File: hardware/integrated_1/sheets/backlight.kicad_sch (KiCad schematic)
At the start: 6 parts

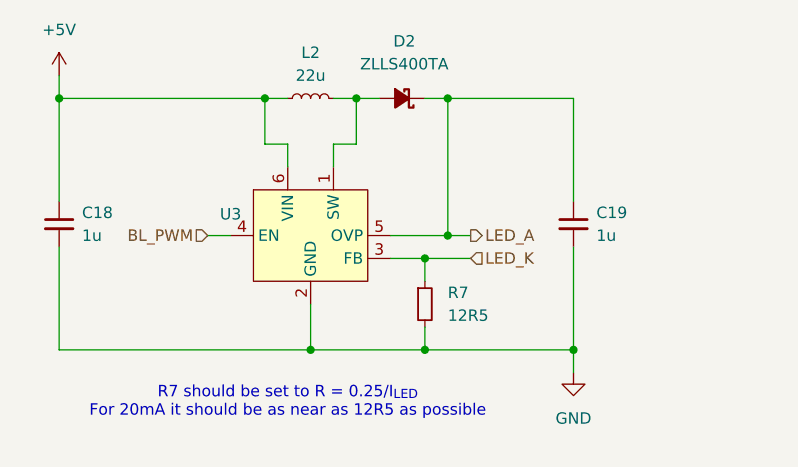
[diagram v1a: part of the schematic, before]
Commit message: automatic kicad reference update
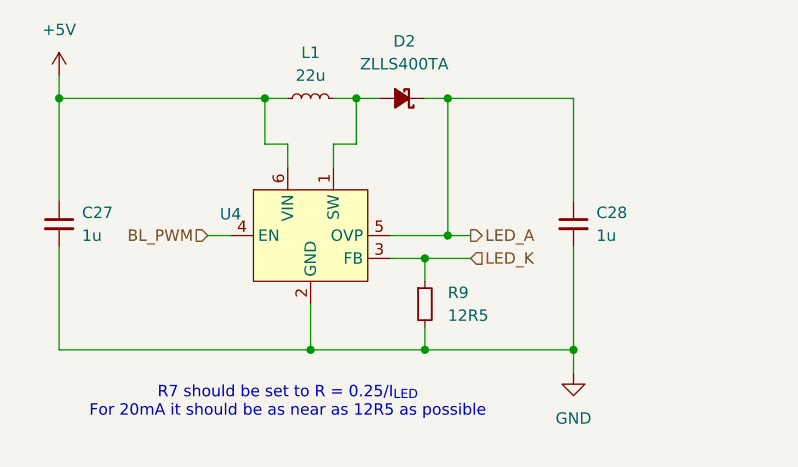
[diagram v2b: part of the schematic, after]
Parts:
- R9: renamed from R7; footprint Resistor_SMD:R_0603_1608Metric -> Resistor_SMD:R_0402_1005Metric
- renumbered C18 to C27, C19 to C28, L2 to L1, U3 to U4
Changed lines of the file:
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@@
 		(dnp no)
 		(fields_autoplaced yes)
-		(property "Reference" "#PWR026"
+		(property "Reference" "#PWR041"
 			(at 336.55 217.17 0)
 			(effects
@@
 			(project "integrated_1"
 				(path "/5cc60e42-d666-4a43-b4f0-3784ee4bf951/7e4f175d-d60a-4b23-9cf2-ca90d4a48e7e"
-					(reference "#PWR026")
+					(reference "#PWR041")
 					(unit 1)
 				)
@@
 		(dnp no)
 		(fields_autoplaced yes)
-		(property "Reference" "C18"
+		(property "Reference" "C27"
 			(at 116.84 93.9862 0)
 			(effects
@@
 			(project "integrated_1"
 				(path "/5cc60e42-d666-4a43-b4f0-3784ee4bf951/7e4f175d-d60a-4b23-9cf2-ca90d4a48e7e"
-					(reference "C18")
+					(reference "C27")
 					(unit 1)
 				)
@@
 		(dnp no)
 		(fields_autoplaced yes)
-		(property "Reference" "R7"
+		(property "Reference" "R9"
 			(at 157.48 102.8699 0)
 			(effects
@@
 			)
 		)
-		(property "Footprint" "Resistor_SMD:R_0603_1608Metric"
+		(property "Footprint" "Resistor_SMD:R_0402_1005Metric"
 			(at 154.94 104.14 0)
 			(effects
@@
 			(project "integrated_1"
 				(path "/5cc60e42-d666-4a43-b4f0-3784ee4bf951/7e4f175d-d60a-4b23-9cf2-ca90d4a48e7e"
-					(reference "R7")
+					(reference "R9")
 					(unit 1)
 				)
@@
 		(dnp no)
 		(fields_autoplaced yes)
-		(property "Reference" "#PWR025"
+		(property "Reference" "#PWR039"
 			(at 114.3 82.55 0)
 			(effects
@@
 			(project "integrated_1"
 				(path "/5cc60e42-d666-4a43-b4f0-3784ee4bf951/7e4f175d-d60a-4b23-9cf2-ca90d4a48e7e"
-					(reference "#PWR025")
+					(reference "#PWR039")
 					(unit 1)
 				)
@@
 		(dnp no)
 		(fields_autoplaced yes)
-		(property "Reference" "#PWR027"
+		(property "Reference" "#PWR040"
 			(at 171.45 118.11 0)
 			(effects
@@
 			(project "integrated_1"
 				(path "/5cc60e42-d666-4a43-b4f0-3784ee4bf951/7e4f175d-d60a-4b23-9cf2-ca90d4a48e7e"
-					(reference "#PWR027")
+					(reference "#PWR040")
 					(unit 1)
 				)
@@
 		(dnp no)
 		(fields_autoplaced yes)
-		(property "Reference" "L2"
+		(property "Reference" "L1"
 			(at 142.24 76.2 90)
 			(effects
@@
 			(project "integrated_1"
 				(path "/5cc60e42-d666-4a43-b4f0-3784ee4bf951/7e4f175d-d60a-4b23-9cf2-ca90d4a48e7e"
-					(reference "L2")
+					(reference "L1")
 					(unit 1)
 				)
@@
 		(dnp no)
 		(fields_autoplaced yes)
-		(property "Reference" "C19"
+		(property "Reference" "C28"
 			(at 173.99 93.9862 0)
 			(effects
@@
 			(project "integrated_1"
 				(path "/5cc60e42-d666-4a43-b4f0-3784ee4bf951/7e4f175d-d60a-4b23-9cf2-ca90d4a48e7e"
-					(reference "C19")
+					(reference "C28")
 					(unit 1)
 				)
@@
 		(dnp no)
 		(fields_autoplaced yes)
-		(property "Reference" "U3"
+		(property "Reference" "U4"
 			(at 133.35 94.142 0)
 			(effects
@@
 			(project "integrated_1"
 				(path "/5cc60e42-d666-4a43-b4f0-3784ee4bf951/7e4f175d-d60a-4b23-9cf2-ca90d4a48e7e"
-					(reference "U3")
-					(unit 1)
-				)
+					(reference "U4")
+					(unit 1)
+				)

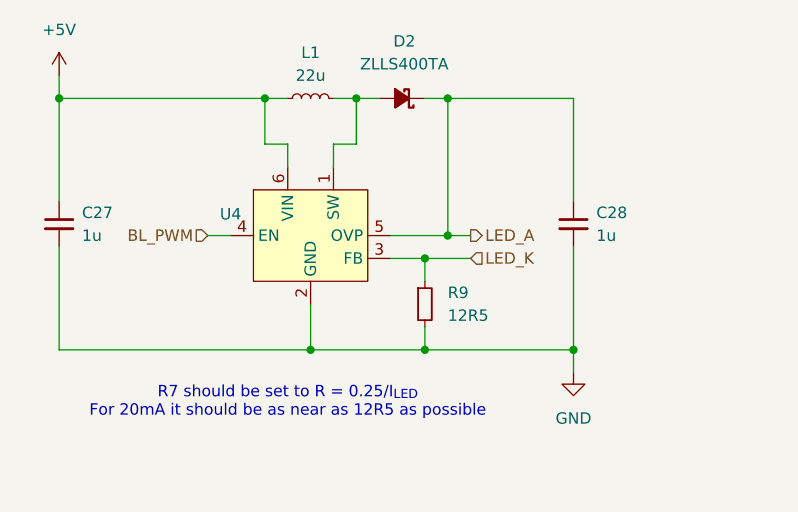
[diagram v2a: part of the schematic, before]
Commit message: reannotated schematic
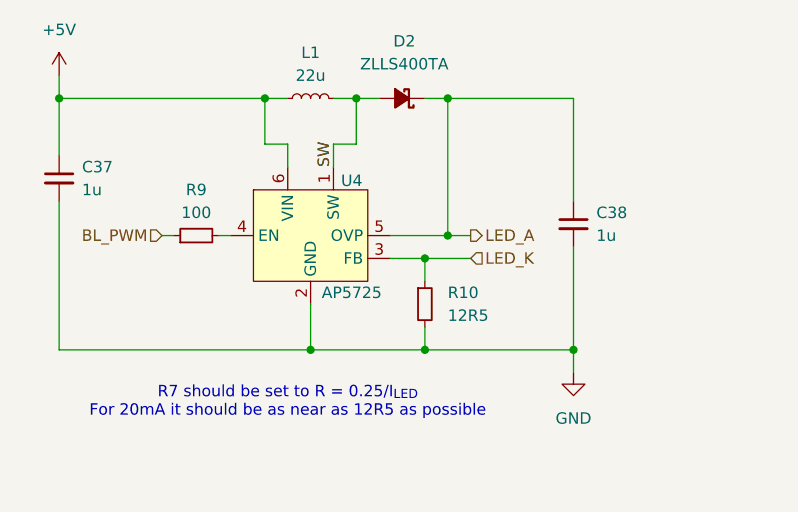
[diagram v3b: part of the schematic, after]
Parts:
- added R9: 100, KiCAD Library:R_0402_1005Metric, symbol Device:R_Small
- C37: renamed from C27; footprint Capacitor_SMD:C_0603_1608Metric -> KiCAD Library:C_0402_1005Metric
- C38: renamed from C28; footprint Capacitor_SMD:C_0603_1608Metric -> KiCAD Library:C_0603_1608Metric
- D2: footprint (none) -> Diode_SMD:D_SOD-323
- L1: footprint (none) -> KiCAD Library:XRNR4012
- R10: renamed from R9; footprint Resistor_SMD:R_0402_1005Metric -> KiCAD Library:R_0402_1005Metric
- U4: value ~ -> AP5725
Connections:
- net BL_PWM: now also R9.1; no longer U4.4 (EN)
- net SW: now reaches D2.2 (A), L1.2, U4.1 (SW)
- new net: R9.2, U4.4 (EN)
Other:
- moved on the sheet: C37
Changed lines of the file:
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@@
 	(wire
 		(pts
-			(xy 130.81 96.52) (xy 133.35 96.52)
+			(xy 125.73 96.52) (xy 127 96.52)
 		)
 		(stroke
@@
 	(wire
 		(pts
-			(xy 114.3 97.79) (xy 114.3 109.22)
+			(xy 114.3 92.71) (xy 114.3 109.22)
 		)
 		(stroke
@@
 	(wire
 		(pts
+			(xy 132.08 96.52) (xy 133.35 96.52)
+		)
+		(stroke
+			(width 0)
+			(type default)
+		)
+	)
+	(wire
+		(pts
 			(xy 171.45 109.22) (xy 154.94 109.22)
 		)
@@
 	(wire
 		(pts
-			(xy 114.3 81.28) (xy 114.3 92.71)
+			(xy 114.3 81.28) (xy 114.3 87.63)
 		)
 		(stroke
@@
 		)
 	)
+	(label "SW"
+		(at 144.78 88.9 90)
+		(fields_autoplaced yes)
+		(effects
+			(font
+				(size 1.27 1.27)
+			)
+			(justify left bottom)
+		)
+	)
 	(hierarchical_label "LED_A"
 		(shape output)
@@
 	(hierarchical_label "BL_PWM"
 		(shape input)
-		(at 130.81 96.52 180)
+		(at 125.73 96.52 180)
 		(fields_autoplaced yes)
 		(effects
@@
 		(dnp no)
 		(fields_autoplaced yes)
-		(property "Reference" "#PWR041"
+		(property "Reference" "#PWR037"
 			(at 336.55 217.17 0)
 			(effects
@@
 			(project "integrated_1"
 				(path "/5cc60e42-d666-4a43-b4f0-3784ee4bf951/7e4f175d-d60a-4b23-9cf2-ca90d4a48e7e"
-					(reference "#PWR041")
+					(reference "#PWR037")
 					(unit 1)
 				)
@@
 			)
 		)
-		(property "Footprint" ""
+		(property "Footprint" "Diode_SMD:D_SOD-323"
 			(at 152.4 81.28 90)
 			(effects
@@
 	(symbol
 		(lib_id "Device:C_Small")
-		(at 114.3 95.25 0)
-		(unit 1)
-		(exclude_from_sim no)
-		(in_bom yes)
-		(on_board yes)
-		(dnp no)
-		(fields_autoplaced yes)
-		(property "Reference" "C27"
-			(at 116.84 93.9862 0)
+		(at 114.3 90.17 0)
+		(unit 1)
+		(exclude_from_sim no)
+		(in_bom yes)
+		(on_board yes)
+		(dnp no)
+		(fields_autoplaced yes)
+		(property "Reference" "C37"
+			(at 116.84 88.9062 0)
 			(effects
 				(font
@@
 		)
 		(property "Value" "1u"
-			(at 116.84 96.5262 0)
+			(at 116.84 91.4462 0)
 			(effects
 				(font
@@
 			)
 		)
-		(property "Footprint" "Capacitor_SMD:C_0603_1608Metric"
-			(at 114.3 95.25 0)
+		(property "Footprint" "KiCAD Library:C_0402_1005Metric"
+			(at 114.3 90.17 0)
 			(effects
 				(font
@@
 		)
 		(property "Datasheet" "~"
-			(at 114.3 95.25 0)
+			(at 114.3 90.17 0)
 			(effects
 				(font
@@
 		)
 		(property "Description" "Unpolarized capacitor, small symbol"
-			(at 114.3 95.25 0)
+			(at 114.3 90.17 0)
 			(effects
 				(font
@@
 			(project "integrated_1"
 				(path "/5cc60e42-d666-4a43-b4f0-3784ee4bf951/7e4f175d-d60a-4b23-9cf2-ca90d4a48e7e"
-					(reference "C27")
+					(reference "C37")
 					(unit 1)
 				)
@@
 		(dnp no)
 		(fields_autoplaced yes)
-		(property "Reference" "R9"
+		(property "Reference" "R10"
 			(at 157.48 102.8699 0)
 			(effects
@@
 			)
 		)
-		(property "Footprint" "Resistor_SMD:R_0402_1005Metric"
+		(property "Footprint" "KiCAD Library:R_0402_1005Metric"
 			(at 154.94 104.14 0)
 			(effects
@@
 		(property "Description" "Resistor, small symbol"
 			(at 154.94 104.14 0)
+			(effects
+				(font
+					(size 1.27 1.27)
+				)
+				(hide yes)
+			)
+		)
+		(pin "2"
+		)
+		(pin "1"
+		)
+		(instances
+			(project "integrated_1"
+				(path "/5cc60e42-d666-4a43-b4f0-3784ee4bf951/7e4f175d-d60a-4b23-9cf2-ca90d4a48e7e"
+					(reference "R10")
+					(unit 1)
+				)
+			)
+		)
+	)
+	(symbol
+		(lib_id "Device:R_Small")
+		(at 129.54 96.52 90)
+		(unit 1)
+		(exclude_from_sim no)
+		(in_bom yes)
+		(on_board yes)
+		(dnp no)
+		(fields_autoplaced yes)
+		(property "Reference" "R9"
+			(at 129.54 91.44 90)
+			(effects
+				(font
+					(size 1.27 1.27)
+				)
+			)
+		)
+		(property "Value" "100"
+			(at 129.54 93.98 90)
+			(effects
+				(font
+					(size 1.27 1.27)
+				)
+			)
+		)
+		(property "Footprint" "KiCAD Library:R_0402_1005Metric"
+			(at 129.54 96.52 0)
+			(effects
+				(font
+					(size 1.27 1.27)
+				)
+				(hide yes)
+			)
+		)
+		(property "Datasheet" "~"
+			(at 129.54 96.52 0)
+			(effects
+				(font
+					(size 1.27 1.27)
+				)
+				(hide yes)
+			)
+		)
+		(property "Description" "Resistor, small symbol"
+			(at 129.54 96.52 0)
 			(effects
 				(font
@@
 		(dnp no)
 		(fields_autoplaced yes)
-		(property "Reference" "#PWR039"
+		(property "Reference" "#PWR035"
 			(at 114.3 82.55 0)
 			(effects
@@
 			(project "integrated_1"
 				(path "/5cc60e42-d666-4a43-b4f0-3784ee4bf951/7e4f175d-d60a-4b23-9cf2-ca90d4a48e7e"
-					(reference "#PWR039")
+					(reference "#PWR035")
 					(unit 1)
 				)
@@
 		(dnp no)
 		(fields_autoplaced yes)
-		(property "Reference" "#PWR040"
+		(property "Reference" "#PWR036"
 			(at 171.45 118.11 0)
 			(effects
@@
 			(project "integrated_1"
 				(path "/5cc60e42-d666-4a43-b4f0-3784ee4bf951/7e4f175d-d60a-4b23-9cf2-ca90d4a48e7e"
-					(reference "#PWR040")
+					(reference "#PWR036")
 					(unit 1)
 				)
@@
 			)
 		)
-		(property "Footprint" ""
+		(property "Footprint" "KiCAD Library:XRNR4012"
 			(at 142.24 81.28 0)
 			(effects
@@
 		(dnp no)
 		(fields_autoplaced yes)
-		(property "Reference" "C28"
+		(property "Reference" "C38"
 			(at 173.99 93.9862 0)
 			(effects
@@
 			)
 		)
-		(property "Footprint" "Capacitor_SMD:C_0603_1608Metric"
+		(property "Footprint" "KiCAD Library:C_0603_1608Metric"
 			(at 171.45 95.25 0)
 			(effects
@@
 			(project "integrated_1"
 				(path "/5cc60e42-d666-4a43-b4f0-3784ee4bf951/7e4f175d-d60a-4b23-9cf2-ca90d4a48e7e"
-					(reference "C28")
+					(reference "C38")
 					(unit 1)
 				)
@@
 		(on_board yes)
 		(dnp no)
-		(fields_autoplaced yes)
 		(property "Reference" "U4"
-			(at 133.35 94.142 0)
-			(effects
-				(font
-					(size 1.27 1.27)
-				)
-			)
-		)
-		(property "Value" "~"
-			(at 133.35 96.0471 0)
-			(effects
-				(font
+			(at 146.812 90.424 0)
+			(effects
+				(font
+					(size 1.27 1.27)
+				)
+			)
+		)
+		(property "Value" "AP5725"
+			(at 146.812 102.87 0)
+			(effects
+				(font

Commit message: reannotated
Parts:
- renumbered C37 to C41, C38 to C42, D2 to D10, R9 to R11, R10 to R12, U4 to U6
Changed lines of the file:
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@@
 		(dnp no)
 		(fields_autoplaced yes)
-		(property "Reference" "#PWR037"
+		(property "Reference" "#PWR048"
 			(at 336.55 217.17 0)
 			(effects
@@
 			(project "integrated_1"
 				(path "/5cc60e42-d666-4a43-b4f0-3784ee4bf951/7e4f175d-d60a-4b23-9cf2-ca90d4a48e7e"
-					(reference "#PWR037")
+					(reference "#PWR048")
 					(unit 1)
 				)
@@
 		(dnp no)
 		(fields_autoplaced yes)
-		(property "Reference" "D2"
+		(property "Reference" "D10"
 			(at 152.654 74.93 0)
 			(effects
@@
 			(project "integrated_1"
 				(path "/5cc60e42-d666-4a43-b4f0-3784ee4bf951/7e4f175d-d60a-4b23-9cf2-ca90d4a48e7e"
-					(reference "D2")
+					(reference "D10")
 					(unit 1)
 				)
@@
 		(dnp no)
 		(fields_autoplaced yes)
-		(property "Reference" "C37"
+		(property "Reference" "C41"
 			(at 116.84 88.9062 0)
 			(effects
@@
 			(project "integrated_1"
 				(path "/5cc60e42-d666-4a43-b4f0-3784ee4bf951/7e4f175d-d60a-4b23-9cf2-ca90d4a48e7e"
-					(reference "C37")
+					(reference "C41")
 					(unit 1)
 				)
@@
 		(dnp no)
 		(fields_autoplaced yes)
-		(property "Reference" "R10"
+		(property "Reference" "R12"
 			(at 157.48 102.8699 0)
 			(effects
@@
 			(project "integrated_1"
 				(path "/5cc60e42-d666-4a43-b4f0-3784ee4bf951/7e4f175d-d60a-4b23-9cf2-ca90d4a48e7e"
-					(reference "R10")
+					(reference "R12")
 					(unit 1)
 				)
@@
 		(dnp no)
 		(fields_autoplaced yes)
-		(property "Reference" "R9"
+		(property "Reference" "R11"
 			(at 129.54 91.44 90)
 			(effects
@@
 			(project "integrated_1"
 				(path "/5cc60e42-d666-4a43-b4f0-3784ee4bf951/7e4f175d-d60a-4b23-9cf2-ca90d4a48e7e"
-					(reference "R9")
+					(reference "R11")
 					(unit 1)
 				)
@@
 		(dnp no)
 		(fields_autoplaced yes)
-		(property "Reference" "#PWR035"
+		(property "Reference" "#PWR046"
 			(at 114.3 82.55 0)
 			(effects
@@
 			(project "integrated_1"
 				(path "/5cc60e42-d666-4a43-b4f0-3784ee4bf951/7e4f175d-d60a-4b23-9cf2-ca90d4a48e7e"
-					(reference "#PWR035")
+					(reference "#PWR046")
 					(unit 1)
 				)
@@
 		(dnp no)
 		(fields_autoplaced yes)
-		(property "Reference" "#PWR036"
+		(property "Reference" "#PWR047"
 			(at 171.45 118.11 0)
 			(effects
@@
 			(project "integrated_1"
 				(path "/5cc60e42-d666-4a43-b4f0-3784ee4bf951/7e4f175d-d60a-4b23-9cf2-ca90d4a48e7e"
-					(reference "#PWR036")
+					(reference "#PWR047")
 					(unit 1)
 				)
@@
 		(dnp no)
 		(fields_autoplaced yes)
-		(property "Reference" "C38"
+		(property "Reference" "C42"
 			(at 173.99 93.9862 0)
 			(effects
@@
 			(project "integrated_1"
 				(path "/5cc60e42-d666-4a43-b4f0-3784ee4bf951/7e4f175d-d60a-4b23-9cf2-ca90d4a48e7e"
-					(reference "C38")
+					(reference "C42")
 					(unit 1)
 				)
@@
 		(on_board yes)
 		(dnp no)
-		(property "Reference" "U4"
+		(property "Reference" "U6"
 			(at 146.812 90.424 0)
 			(effects
@@
 			(project "integrated_1"
 				(path "/5cc60e42-d666-4a43-b4f0-3784ee4bf951/7e4f175d-d60a-4b23-9cf2-ca90d4a48e7e"
-					(reference "U4")
-					(unit 1)
-				)
+					(reference "U6")
+					(unit 1)
+				)

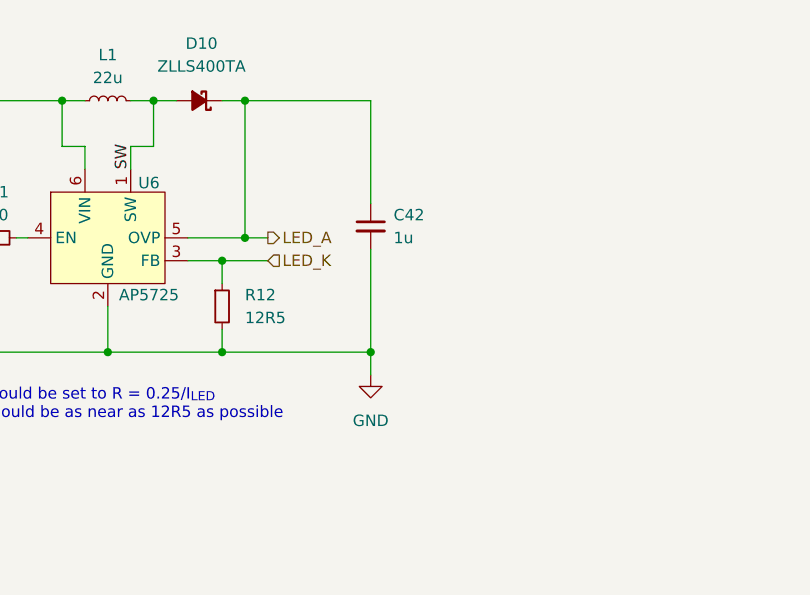
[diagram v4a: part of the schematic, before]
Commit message: added testpoints
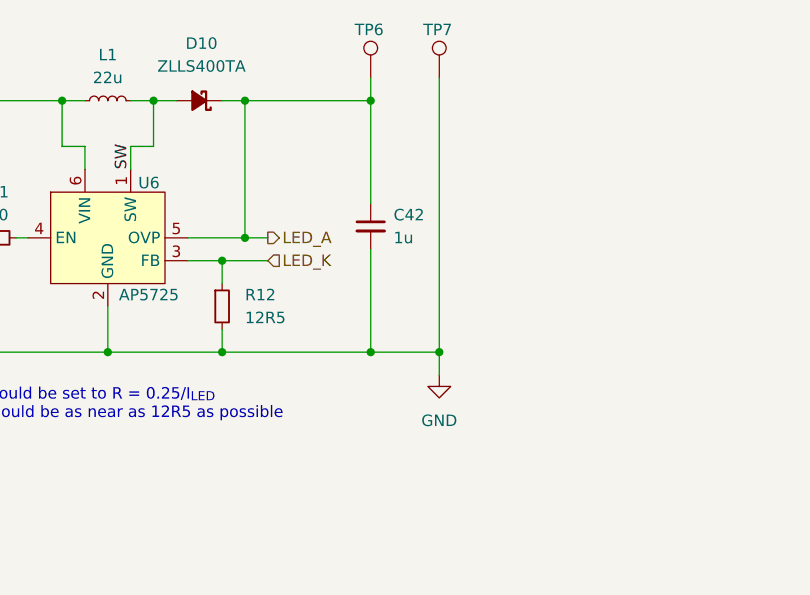
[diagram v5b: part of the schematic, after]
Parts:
- added TP6, TP7: TestPoint, TestPoint:TestPoint_Pad_D1.0mm, symbol Connector:TestPoint
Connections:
- net GND: now also TP7.1
- net LED_A: now also TP6.1
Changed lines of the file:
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@@
+	)
+	(junction
+		(at 179.07 109.22)
+		(diameter 0)
+		(color 0 0 0 0)
 	)
 	(junction
@@
 	)
 	(junction
+		(at 171.45 81.28)
+		(diameter 0)
+		(color 0 0 0 0)
+	)
+	(junction
 		(at 154.94 99.06)
 		(diameter 0)
@@
 	(wire
 		(pts
-			(xy 171.45 111.76) (xy 171.45 109.22)
+			(xy 179.07 111.76) (xy 179.07 109.22)
 		)
 		(stroke
@@
 	(wire
 		(pts
+			(xy 171.45 78.74) (xy 171.45 81.28)
+		)
+		(stroke
+			(width 0)
+			(type default)
+		)
+	)
+	(wire
+		(pts
 			(xy 151.13 96.52) (xy 157.48 96.52)
 		)
@@
 	(wire
 		(pts
+			(xy 179.07 78.74) (xy 179.07 109.22)
+		)
+		(stroke
+			(width 0)
+			(type default)
+		)
+	)
+	(wire
+		(pts
 			(xy 114.3 109.22) (xy 142.24 109.22)
 		)
@@
 		(pts
 			(xy 144.78 86.36) (xy 147.32 86.36)
+		)
+		(stroke
+			(width 0)
+			(type default)
+		)
+	)
+	(wire
+		(pts
+			(xy 179.07 109.22) (xy 171.45 109.22)
 		)
 		(stroke
@@
 	)
 	(symbol
+		(lib_id "Connector:TestPoint")
+		(at 179.07 78.74 0)
+		(unit 1)
+		(exclude_from_sim no)
+		(in_bom yes)
+		(on_board yes)
+		(dnp no)
+		(property "Reference" "TP7"
+			(at 177.292 73.406 0)
+			(effects
+				(font
+					(size 1.27 1.27)
+				)
+				(justify left)
+			)
+		)
+		(property "Value" "TestPoint"
+			(at 181.61 76.7079 0)
+			(effects
+				(font
+					(size 1.27 1.27)
+				)
+				(justify left)
+				(hide yes)
+			)
+		)
+		(property "Footprint" "TestPoint:TestPoint_Pad_D1.0mm"
+			(at 184.15 78.74 0)
+			(effects
+				(font
+					(size 1.27 1.27)
+				)
+				(hide yes)
+			)
+		)
+		(property "Datasheet" "~"
+			(at 184.15 78.74 0)
+			(effects
+				(font
+					(size 1.27 1.27)
+				)
+				(hide yes)
+			)
+		)
+		(property "Description" "test point"
+			(at 179.07 78.74 0)
+			(effects
+				(font
+					(size 1.27 1.27)
+				)
+				(hide yes)
+			)
+		)
+		(pin "1"
+		)
+		(instances
+			(project "integrated_1"
+				(path "/5cc60e42-d666-4a43-b4f0-3784ee4bf951/7e4f175d-d60a-4b23-9cf2-ca90d4a48e7e"
+					(reference "TP7")
+					(unit 1)
+				)
+			)
+		)
+	)
+	(symbol
 		(lib_id "Device:D_Schottky_Small_Filled")
 		(at 152.4 81.28 180)
@@
 	(symbol
 		(lib_id "PCM_4ms_Power-symbol:GND")
-		(at 171.45 111.76 0)
+		(at 179.07 111.76 0)
 		(unit 1)
 		(exclude_from_sim no)
@@
 		(fields_autoplaced yes)
 		(property "Reference" "#PWR047"
-			(at 171.45 118.11 0)
+			(at 179.07 118.11 0)
 			(effects
 				(font
@@
 		)
 		(property "Value" "GND"
-			(at 171.45 116.84 0)
+			(at 179.07 116.84 0)
 			(effects
 				(font
@@
 		)
 		(property "Footprint" ""
-			(at 171.45 111.76 0)
+			(at 179.07 111.76 0)
 			(effects
 				(font
@@
 		)
 		(property "Datasheet" ""
-			(at 171.45 111.76 0)
+			(at 179.07 111.76 0)
 			(effects
 				(font
@@
 		)
 		(property "Description" ""
-			(at 171.45 111.76 0)
+			(at 179.07 111.76 0)
 			(effects
 				(font
@@
 					(unit 1)
 				)
+			)
+		)
+	)
+	(symbol
+		(lib_id "Connector:TestPoint")
+		(at 171.45 78.74 0)
+		(unit 1)
+		(exclude_from_sim no)
+		(in_bom yes)
+		(on_board yes)
+		(dnp no)
+		(property "Reference" "TP6"
+			(at 169.672 73.406 0)
+			(effects
+				(font
+					(size 1.27 1.27)
+				)
+				(justify left)
+			)
+		)
+		(property "Value" "TestPoint"
+			(at 173.99 76.7079 0)
+			(effects
+				(font
+					(size 1.27 1.27)
+				)
+				(justify left)
+				(hide yes)
+			)
+		)
+		(property "Footprint" "TestPoint:TestPoint_Pad_D1.0mm"
+			(at 176.53 78.74 0)
+			(effects
+				(font
+					(size 1.27 1.27)
+				)
+				(hide yes)
+			)
+		)
+		(property "Datasheet" "~"
+			(at 176.53 78.74 0)
+			(effects
+				(font
+					(size 1.27 1.27)
+				)
+				(hide yes)
+			)
+		)
+		(property "Description" "test point"
+			(at 171.45 78.74 0)
+			(effects
+				(font
+					(size 1.27 1.27)
+				)
+				(hide yes)
+			)
+		)
+		(pin "1"
+		)
+		(instances
+			(project "integrated_1"
+				(path "/5cc60e42-d666-4a43-b4f0-3784ee4bf951/7e4f175d-d60a-4b23-9cf2-ca90d4a48e7e"
+					(reference "TP6")
+					(unit 1)
+				)

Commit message: exported 3d models + added date stamp
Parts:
- R12: footprint KiCAD Library:R_0402_1005Metric -> KiCAD Library:R_0603_1608Metric
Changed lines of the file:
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@@
 			)
 		)
-		(property "Footprint" "KiCAD Library:R_0402_1005Metric"
+		(property "Footprint" "KiCAD Library:R_0603_1608Metric"
 			(at 154.94 104.14 0)
 			(effects
